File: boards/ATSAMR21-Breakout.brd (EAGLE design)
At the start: 27.6 x 50.8 mm, 20 parts, among them IC1 MCP73831T-2ATI/OT, IC2 LTC4412, IC3 NCP4589DSN33T1G, IC4 ATSAMR21G18-MR210UA, Q1 SI2301CDS-T1-GE3

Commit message: Added breakout board for ATZB-RF-233-1-C.
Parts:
- C1: value TPSB107M010R0400 -> 10uF
- C2: value TPSB107M010R0400 -> 47uF
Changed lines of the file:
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@@
 <?xml version="1.0" encoding="utf-8"?>
 <!DOCTYPE eagle SYSTEM "eagle.dtd">
-<eagle version="7.4.0">
+<eagle version="7.7.0">
 <drawing>
 <settings>
@@
 <attribute name="NAME" x="14.224" y="11.1125" size="0.8128" layer="25" font="vector" ratio="16" rot="R90"/>
 </element>
-<element name="C1" library="custom_componentsv0.9" package="1210-POLARIZED" value="TPSB107M010R0400" x="11.938" y="8.636" smashed="yes" rot="R270">
+<element name="C1" library="custom_componentsv0.9" package="1210-POLARIZED" value="10uF" x="11.938" y="8.636" smashed="yes" rot="R270">
 <attribute name="NAME" x="13.462" y="9.398" size="0.8128" layer="25" font="vector" ratio="15" rot="R270"/>
 </element>
-<element name="C2" library="custom_componentsv0.9" package="1210-POLARIZED" value="TPSB107M010R0400" x="12.446" y="19.304" smashed="yes" rot="R270">
+<element name="C2" library="custom_componentsv0.9" package="1210-POLARIZED" value="47uF" x="12.446" y="19.304" smashed="yes" rot="R270">
 <attribute name="NAME" x="11.684" y="16.002" size="0.8128" layer="25" font="vector" ratio="16"/>
 </element>

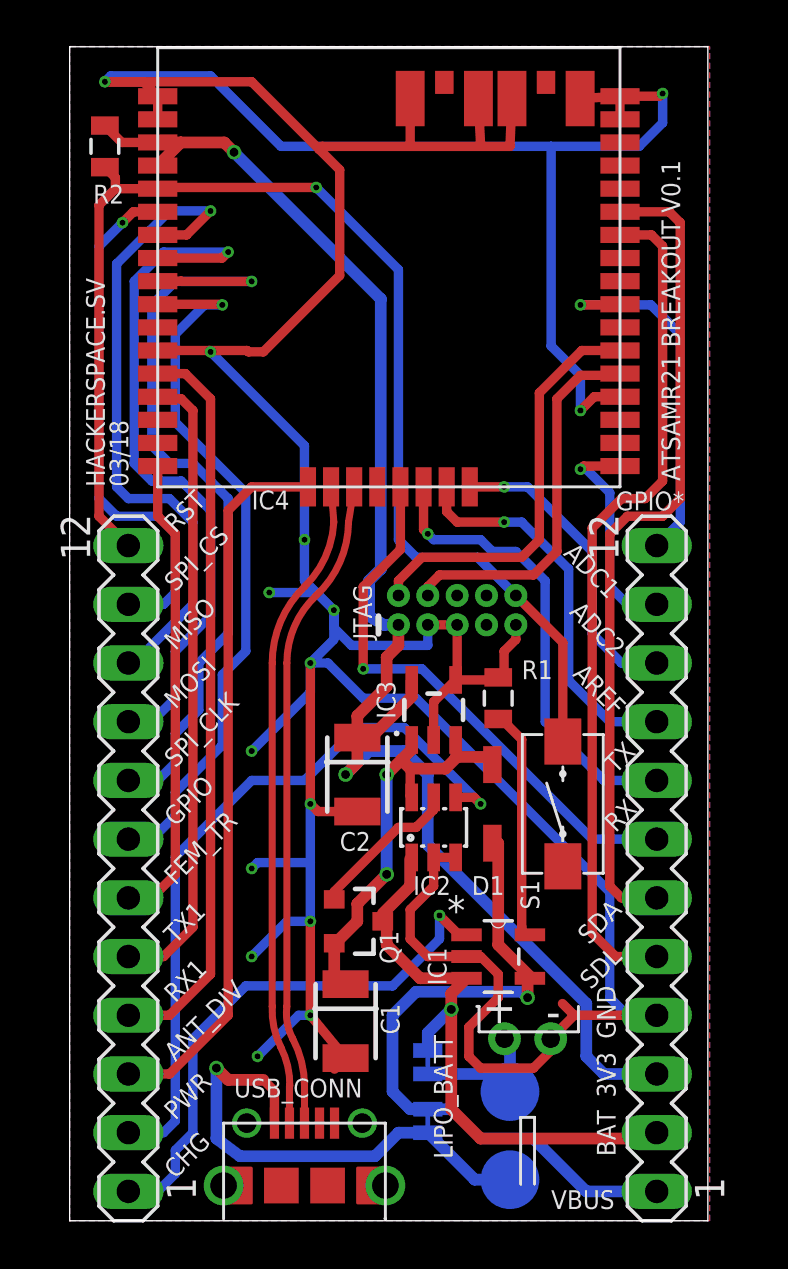
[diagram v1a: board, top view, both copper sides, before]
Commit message: Changed Power-Path design.
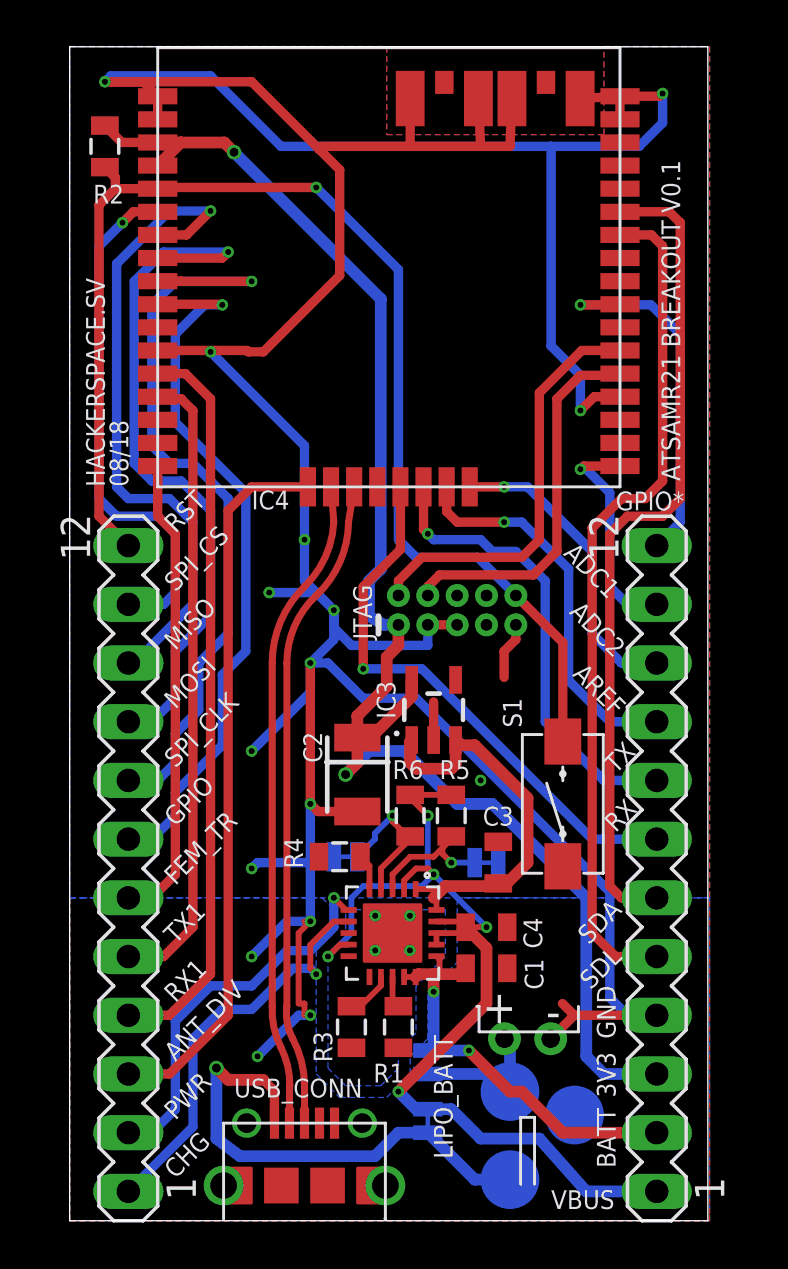
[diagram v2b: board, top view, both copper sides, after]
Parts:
- removed D1: 1N5819HW-7-F, custom_components:SOD123
- removed IC1: MCP73831T-2ATI/OT, custom_components:SOT95P300X145-5N
- removed IC2: LTC4412, custom_components:SOT23-6L
- removed Q1: SI2301CDS-T1-GE3, SparkFun-DiscreteSemi:SOT23-3
- added C3: 4.7uF, SparkFun-Capacitors:0805
- added C4: 10uF, SparkFun-Capacitors:0805
- added R3: 100K, SparkFun-Resistors:0805
- added R4, R5, R6: 10K, SparkFun-Resistors:0805
- added SJ3, SJ4: SOLDERJUMPERTRACE, SparkFun-Retired:SJ_2S-TRACE
- added TP3: TPB2,54, testpad:B2,54
- added U$1: MCP73871T, radios:QFN-20
- C1: value 10uF -> 4.7uF; device custom_componentsv0.9:1210-POLARIZED -> SparkFun-Capacitors:0805
- R1: value 10K -> 2K
- moved R1 14.9 mm to (14.2, 8.38), turned to 90 degrees
- moved C1 6.51 mm to (18.0, 10.9), turned to 0 degrees
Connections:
- removed net N$8: IC1.5, R1.2
- new net N$2: R5.1, SJ4.2, U$1.3
- new net N$3: R3.2, U$1.12
- new net N$4: R1.2, U$1.13
- new net N$5: R4.2, U$1.5
- new net THERMAL: U$1.EP$1, U$1.EP$2, U$1.EP$3, U$1.EP$4
- net CHG_STATUS: now also U$1.7; no longer IC1.1
- net GND: now also C3.2, C4.2, R3.1, R4.1, SJ3.1, SJ4.1, TP3.TP, U$1.10, U$1.11; no longer IC1.2, IC2.2, IC2.3, IC3.4
- net N$1: now also R6.1, SJ3.2, U$1.4; no longer IC2.5, Q1.1
- net PWR_STAT: now also U$1.6; no longer IC2.4
- net VBATT: now also C1.1, U$1.14, U$1.15, U$1.16; no longer IC1.3, IC2.1, Q1.3
- net VBUS: now also C4.1, R5.2, R6.2, U$1.17, U$1.18, U$1.19, U$1.2, U$1.9; no longer D1.2, IC1.4
- net VIN: now also C3.1, U$1.1, U$1.20; no longer C1.1, D1.1, IC2.6, Q1.2
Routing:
- net GND: track 206.8 -> 180.8 mm, vias 15 -> 16
- net PWR_STAT: track 31.8 -> 16.9 mm
- net VBUS: track 30.4 -> 45.1 mm, vias 1 -> 5
- net N$8: track 9.99 -> 0.00 mm
- net VBATT: track 26.1 -> 18.4 mm, vias 1 -> 2
- net N$2: track 0.00 -> 5.74 mm, vias 0 -> 1
- net CHG_STATUS: track 23.5 -> 17.9 mm
- net N$3: track 0.00 -> 2.02 mm
- net N$5: track 0.00 -> 1.56 mm
- net VIN: track 19.1 -> 17.6 mm, vias 2 -> 0
- net N$4: track 0.00 -> 1.37 mm
- net 3.3V: track 66.5 -> 67.4 mm
- net N$1: track 6.64 -> 6.54 mm, vias 0 -> 1
- added copper zone on layer 16, net THERMAL
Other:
- board text added: "08/18"
- board text added: "Cut SJ1 to power using VBUS pin"
- board text added: "Cut SJ2 to disconnect battery"
- board text added: "Cut SJ3 & SJ4 to charge battery at 500mA. With jumpers closed it will be limited to 100mA."
- board text removed: "03/18"
- board text removed: "BAT"
